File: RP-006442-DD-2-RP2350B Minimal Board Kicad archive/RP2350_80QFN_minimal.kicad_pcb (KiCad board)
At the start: 2 copper layers, 99.4 x 99.4 mm, 164 parts, among them J1 USB_C_Receptacle_USB2.0_16P, J2 Conn_02x14_Odd_Even, J3 Conn_02x09_Odd_Even, J4 Conn_01x03, J5 USB_C_Receptacle_USB2.0_16P, J6 Conn_01x05, SW1 SW_Push, SW10 SW_DIP_x08, SW2 SW_Push, SW3 SW_Push, SW4 SW_Push, SW5 SW_Push, SW6 SW_Push, SW7 SW_Push, SW8 SW_Push, SW9 SW_SPDT, U1 RP2350_80QFN, U10 74HC595, U11 74HC595, U12 LIS2DW12TR, U13 74HC595, U2 NCP1117-3.3_SOT223, U3 W25Q128JVS, U4 DNF, U5 W25Q128JVS, U6 NCP1117-3.3_SOT223, U7 RP2350_60QFN, U8 HT16K33A-24SSOP, U9 CC56-12EWA, Y1 ABM8-272-T3, Y2 ABM8-272-T3

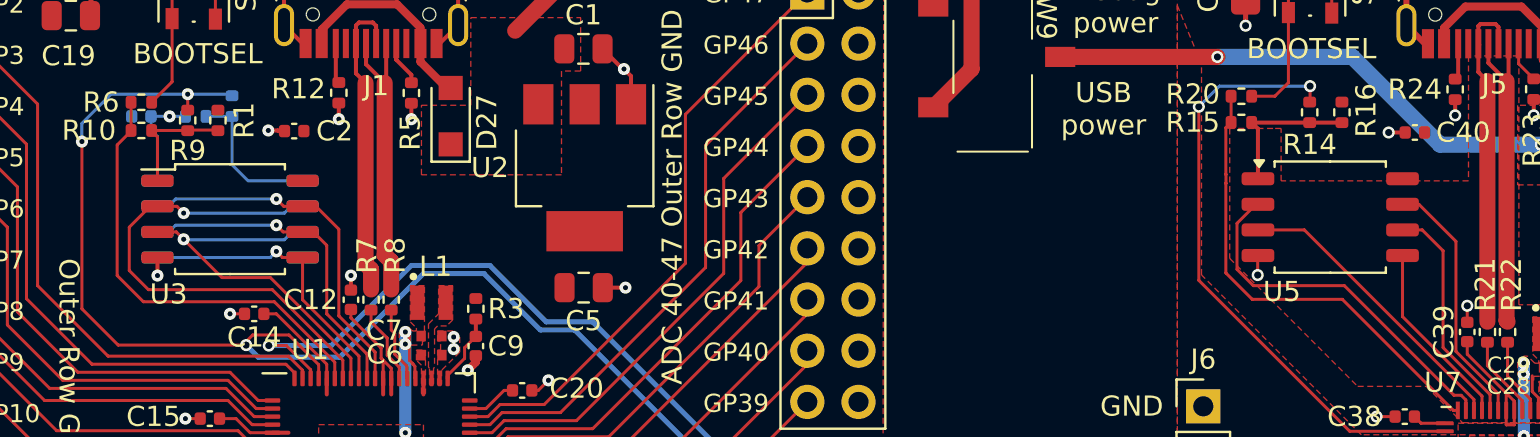
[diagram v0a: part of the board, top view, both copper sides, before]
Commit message: New Flash memory footprint
footprint from snapmagic
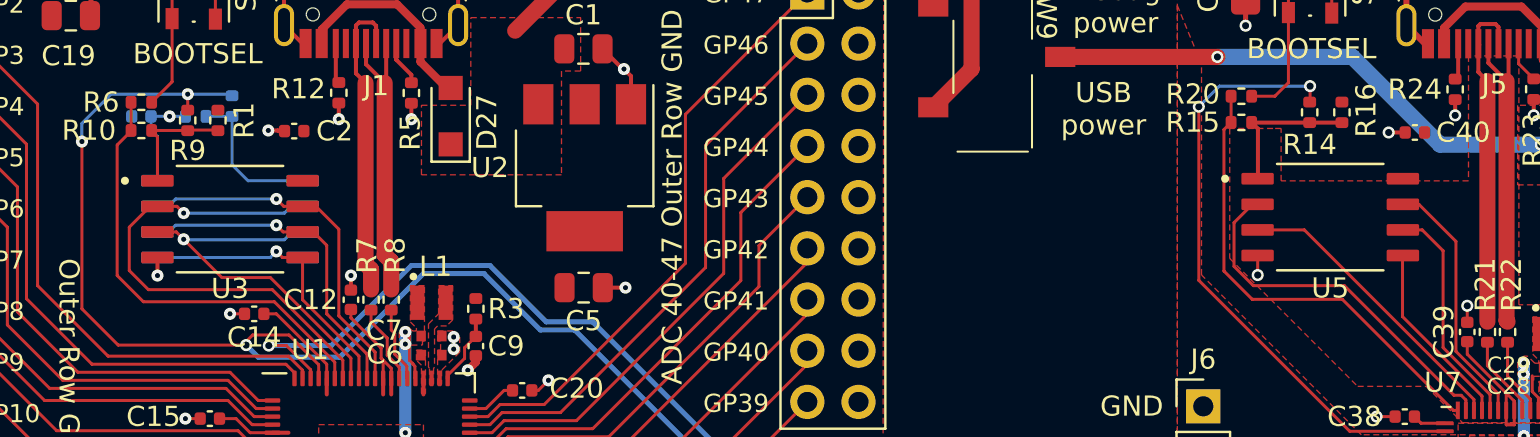
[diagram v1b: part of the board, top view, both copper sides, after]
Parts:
- U3, U4: footprint Package_SO:SOIC-8_5.23x5.23mm_P1.27mm -> W25Q128JVSIQ:SOIC127P790X216-8N
- U5: footprint Package_SO:SOIC-8_5.3x5.3mm_P1.27mm -> W25Q128JVSIQ:SOIC127P790X216-8N

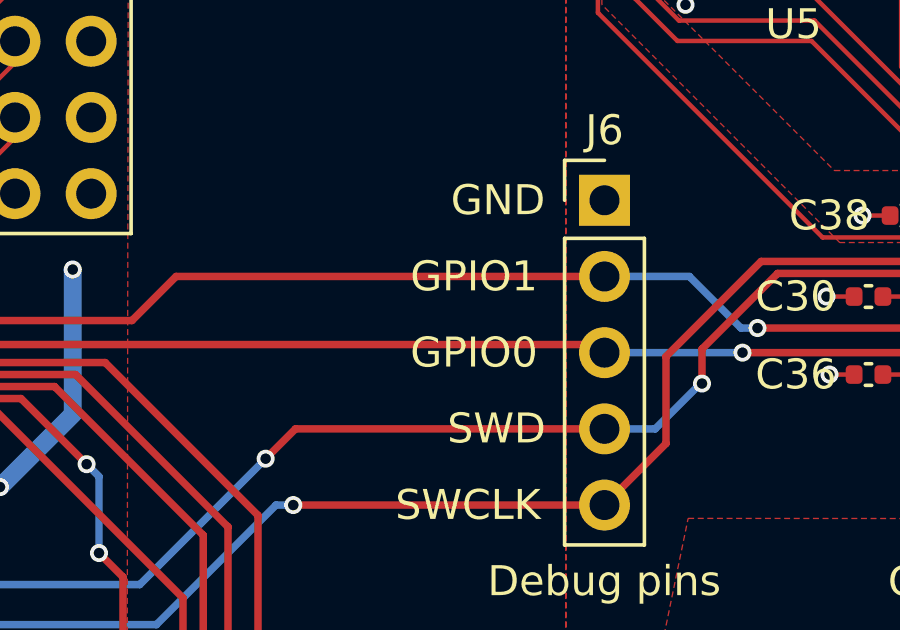
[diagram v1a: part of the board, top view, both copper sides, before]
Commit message: Added MMA8451QR1 symbol and footprint
MMA8451QR1 Accelerometer
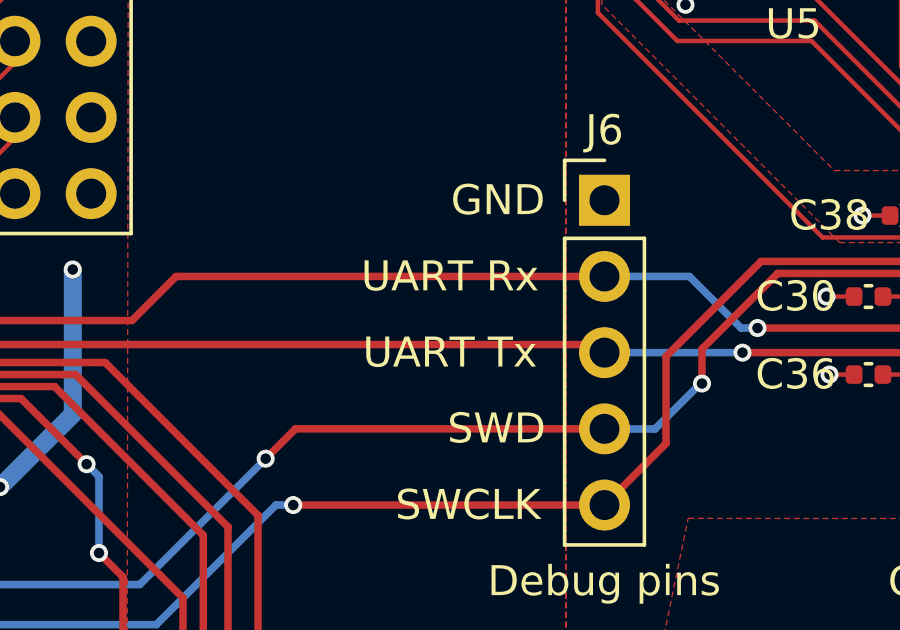
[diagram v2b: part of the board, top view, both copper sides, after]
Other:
- board text added: "UART Rx"
- board text added: "UART Tx"
- board text removed: "GPIO0"
- board text removed: "GPIO1"
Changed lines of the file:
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@@
 		)
 	)
-	(gr_text "GPIO1"
-		(at 124.8 74.08 0)
+	(gr_text "UART Rx"
+		(at 124 74.08 0)
 		(layer "F.SilkS")
 		(effects
@@
 		)
 	)
-	(gr_text "GPIO0"
-		(at 124.8 76.62 0)
+	(gr_text "UART Tx"
+		(at 124 76.62 0)
 		(layer "F.SilkS")
 		(effects

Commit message: Update RP2350_80QFN_minimal.kicad_pcb
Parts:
- removed the C42 at (70.0, 95.7)
- removed the U12 at (75.2, 90.9)
- added U13: MMA8451QR1, MMA8451QR1:QFN50P300X300X100-16N, F.Cu at (72.5, 115.5)
- C45: value 100n -> 4.7u
- C47: value 10u -> 100n
- moved C45 25.9 mm to (75.5, 116.0)
- moved C42 24.5 mm to (74.5, 113.0), turned to 0 degrees
- moved C47 23.9 mm to (73.0, 112.5), turned to 90 degrees
- renumbered C46 to C42, U13 to U12
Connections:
- C42 pad 1: Net-(U12-VDD_IO) -> +3V3
- C45 pad 1: Net-(U12-VDD_IO) -> +3V3
- C47 pad 1: Net-(U12-VDD_IO) -> Net-(U13-BYP)
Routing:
- net /GPIO18: track 18.3 -> 55.2 mm, vias 2 -> 4
- net /GPIO19: track 17.0 -> 49.5 mm, vias 2 -> 4
- net /GPIO20: track 50.5 -> 57.8 mm, vias 2 -> 0
- net +3V3: track 175.4 -> 182.5 mm, vias 17 -> 15
- net /GPIO21: track 48.3 -> 55.3 mm, vias 2 -> 4
- net Net-(U12-VDD_IO): track 4.34 -> 0.00 mm
- net GND: track 175.5 -> 179.2 mm, vias 104 -> 106
- net Net-(U13-BYP): track 0.00 -> 1.25 mm

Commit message: Update pcb
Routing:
- net +3V3: track 182.5 -> 185.0 mm, vias 15 -> 17
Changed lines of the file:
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@@
 			(psa4output no)
 			(plot_black_and_white yes)
+			(plotinvisibletext no)
 			(sketchpadsonfab no)
 			(plotpadnumbers no)
@@
 			(keep_text_aligned yes)
 		)
-		(gr_text "12,7000 mm"
+		(gr_text "12.7000 mm"
 			(at 92.35 148.2725 0)
 			(layer "Cmts.User")
@@
 			(keep_text_aligned yes)
 		)
-		(gr_text "2,0000 mm"
+		(gr_text "2.0000 mm"
 			(at 63.95 117.8 90)
 			(layer "Cmts.User")
@@
 			(keep_text_aligned yes)
 		)
-		(gr_text "17,7700 mm"
+		(gr_text "17.7700 mm"
 			(at 87.185 101.3 0)
 			(layer "Cmts.User")
@@
 			(keep_text_aligned yes)
 		)
-		(gr_text "10,4000 mm"
+		(gr_text "10.4000 mm"
 			(at 104.31 102.45 90)
 			(layer "Cmts.User")
@@
 			(keep_text_aligned yes)
 		)
-		(gr_text "50,3000 mm"
+		(gr_text "50.3000 mm"
 			(at 92.35 144.32 0)
 			(layer "Cmts.User")
@@
 			(keep_text_aligned yes)
 		)
-		(gr_text "19,0000 mm"
+		(gr_text "19.0000 mm"
 			(at 69.84 130.38 90)
 			(layer "Cmts.User")
@@
 			(keep_text_aligned yes)
 		)
-		(gr_text "2,5400 mm"
+		(gr_text "2.5400 mm"
 			(at 79.57 96.22 0)
 			(layer "Cmts.User")
@@
 			(keep_text_aligned yes)
 		)
-		(gr_text "7,4000 mm"
+		(gr_text "7.4000 mm"
 			(at 100.68 102.45 90)
 			(layer "Cmts.User")
@@
 			(keep_text_aligned yes)
 		)
-		(gr_text "15,2275 mm"
+		(gr_text "15.2275 mm"
 			(at 79.325 130.38625 90)
 			(layer "Cmts.User")
@@
 			(keep_text_aligned yes)
 		)
-		(gr_text "100,0000 mm"
+		(gr_text "100.0000 mm"
 			(at 180.55 95.05 90)
 			(layer "Cmts.User")
@@
 			(keep_text_aligned yes)
 		)
-		(gr_text "99,4000 mm"
+		(gr_text "99.4000 mm"
 			(at 111.85 36.55 0)
 			(layer "Cmts.User")
@@
 			(keep_text_aligned yes)
 		)
-		(gr_text "5,0000 mm"
+		(gr_text "5.0000 mm"
 			(at 74.1 142.5 90)
 			(layer "Cmts.User")
@@
 	)
 	(segment
-		(start 70.53 95.7)
-		(end 70.53 96.92)
-		(width 0.25)
-		(layer "F.Cu")
-		(net 5)
-	)
-	(segment
 		(start 85.25 79.9465)
 		(end 85.25 79.15)
@@
 	)
 	(segment
+		(start 70.53 95.5)
+		(end 69.58 94.55)
+		(width 0.25)
+		(layer "F.Cu")
+		(net 5)
+	)
+	(segment
 		(start 75.663806 115.414)
 		(end 76.286 115.414)
@@
 	)
 	(segment
-		(start 70.53 95.5)
-		(end 69.58 94.55)
-		(width 0.25)
-		(layer "F.Cu")
-		(net 5)
-	)
-	(segment
 		(start 112.95 116.97)
 		(end 122.75 126.77)
@@
 	)
 	(segment
-		(start 70.53 95.7)
-		(end 70.53 95.5)
-		(width 0.15)
-		(layer "F.Cu")
-		(net 5)
-	)
-	(segment
 		(start 84.5 57.9)
 		(end 84.52 57.88)
@@
 	)
 	(segment
+		(start 70.53 96.92)
+		(end 70.53 95.5)
+		(width 0.25)
+		(layer "F.Cu")
+		(net 5)
+	)
+	(segment
 		(start 144.58223 72.46)
 		(end 144.58223 71.7415)
@@
 	)
 	(segment
-		(start 70.53 96.92)
-		(end 70.35 97.1)
-		(width 0.25)
-		(layer "F.Cu")
-		(net 5)
-	)
-	(segment
 		(start 144.18223 71.7415)
 		(end 144.18223 72.45223)
@@
 	)
 	(via
+		(at 76.55 110.55)
+		(size 0.6)
+		(drill 0.35)
+		(layers "F.Cu" "B.Cu")
+		(free yes)
+		(net 5)
+	)
+	(via
 		(at 107.25 80.25)
 		(size 0.6)
@@
 	)
 	(via
-		(at 77.45 91.6)
+		(at 107.625 97.825)
 		(size 0.6)
 		(drill 0.35)
@@
 	)
 	(via
-		(at 107.625 97.825)
+		(at 71.1 98.05)
 		(size 0.6)
 		(drill 0.35)
@@
 	)
 	(via
-		(at 77.45 85.65)
+		(at 76.55 106.975)
 		(size 0.6)
 		(drill 0.35)
 		(layers "F.Cu" "B.Cu")
+		(free yes)
 		(net 5)
 	)
@@
 	)
 	(via
+		(at 76.275 98.05)
+		(size 0.6)
+		(drill 0.35)
+		(layers "F.Cu" "B.Cu")
+		(free yes)
+		(net 5)
+	)
+	(via
 		(at 149.45 50.1)
 		(size 0.6)
@@
 	)
 	(segment
-		(start 77.45 91.6)
-		(end 77.45 85.65)
+		(start 76.55 110.55)
+		(end 76.55 106.975)
 		(width 0.6)
 		(layer "B.Cu")
@@
 	)
 	(segment
+		(start 71.1 98.05)
+		(end 76.275 98.05)
+		(width 0.6)
+		(layer "B.Cu")
+		(net 5)
+	)
+	(segment
 		(start 81.35 83.55)
 		(end 78.85 83.55)
@@
 	)
 	(segment
-		(start 111.3 109.55)
-		(end 112.35 109.55)
+		(start 77.575 101.75)
+		(end 99.15 101.75)
 		(width 0.25)
 		(layer "F.Cu")
@@
 	)
 	(segment
-		(start 66.525 86.925)
-		(end 66.525 94.75)
+		(start 111.3 109.55)
+		(end 112.35 109.55)
 		(width 0.25)
 		(layer "F.Cu")
@@
 	)
 	(segment
-		(start 99.15 101.75)
-		(end 76.2 101.75)
+		(start 66.525 86.925)
+		(end 66.525 94.75)
 		(width 0.25)
 		(layer "F.Cu")
@@
 	)
 	(via
-		(at 76.2 101.75)
+		(at 77.575 101.75)
 		(size 0.6)
 		(drill 0.35)
@@
 	)
 	(segment
-		(start 106.25 101.75)
-		(end 111.3 106.8)
+		(start 69.875 101.75)
+		(end 66.525 98.4)
 		(width 0.25)
 		(layer "B.Cu")
@@
 	)
 	(segment
-		(start 99.15 101.75)
-		(end 106.25 101.75)
+		(start 106.25 101.75)
+		(end 111.3 106.8)
 		(width 0.25)
 		(layer "B.Cu")
@@
 	)
 	(segment
-		(start 111.3 106.8)
-		(end 111.3 109.55)
+		(start 66.525 98.4)
+		(end 66.525 94.75)
 		(width 0.25)
 		(layer "B.Cu")
@@
 	)
 	(segment
-		(start 76.2 101.75)
-		(end 69.875 101.75)
+		(start 99.15 101.75)
+		(end 106.25 101.75)
 		(width 0.25)
 		(layer "B.Cu")
@@
 	)
 	(segment
-		(start 69.875 101.75)
-		(end 66.525 98.4)
+		(start 77.575 101.75)
+		(end 69.875 101.75)
 		(width 0.25)
 		(layer "B.Cu")
@@
 	)
 	(segment
-		(start 66.525 98.4)
-		(end 66.525 94.75)
+		(start 111.3 106.8)
+		(end 111.3 109.55)
 		(width 0.25)
 		(layer "B.Cu")
@@
 	)
 	(segment
+		(start 99.1 100.025)
+		(end 77.525 100.025)
+		(width 0.25)
+		(layer "F.Cu")
+		(net 32)
+	)
+	(segment
 		(start 111.325 100.025)
 		(end 112.375 100.025)
@@
 	)
 	(segment
-		(start 99.1 100.025)
-		(end 76.2 100.025)
-		(width 0.25)
-		(layer "F.Cu")
-		(net 32)
-	)
-	(segment
 		(start 67.8 96.05)
 		(end 67.8 88.25)
@@
 	)
 	(via
-		(at 76.2 100.025)
+		(at 77.525 100.025)
 		(size 0.6)
 		(drill 0.35)
@@
 	)
 	(segment
-		(start 67.8 97.125)
-		(end 67.8 96.05)
+		(start 70.7 100.025)
+		(end 67.8 97.125)
 		(width 0.25)
 		(layer "B.Cu")
@@
 	)
 	(segment
-		(start 70.7 100.025)
-		(end 67.8 97.125)
+		(start 77.525 100.025)
+		(end 70.7 100.025)
 		(width 0.25)
 		(layer "B.Cu")
@@
 	)
 	(segment
-		(start 76.2 100.025)
-		(end 70.7 100.025)
+		(start 67.8 97.125)
+		(end 67.8 96.05)
 		(width 0.25)
 		(layer "B.Cu")
@@
 	)
 	(segment
+		(start 77.475 100.825)
+		(end 99.1 100.825)
+		(width 0.25)
+		(layer "F.Cu")
+		(net 33)
+	)
+	(segment
 		(start 112.35 105)
 		(end 112.375 105.025)
@@
 	)
 	(segment
-		(start 67.15 95.5)
-		(end 67.15 87.6)
-		(width 0.25)
-		(layer "F.Cu")
-		(net 33)
-	)
-	(segment
 		(start 99.1 100.825)
 		(end 99.125 100.85)
@@
 	)
 	(segment
-		(start 76.2 100.825)
-		(end 99.1 100.825)
+		(start 67.15 95.5)
+		(end 67.15 87.6)
 		(width 0.25)
 		(layer "F.Cu")
@@
 	)
 	(via
-		(at 76.2 100.825)
+		(at 77.475 100.825)
 		(size 0.6)
 		(drill 0.35)
@@
 	)
 	(segment
-		(start 107.2 100.85)
-		(end 111.35 105)
+		(start 67.15 97.85)
+		(end 67.15 95.5)
 		(width 0.25)
 		(layer "B.Cu")
@@
 	)
 	(segment
-		(start 70.125 100.825)
-		(end 67.15 97.85)
+		(start 107.2 100.85)
+		(end 111.35 105)
 		(width 0.25)
 		(layer "B.Cu")
@@
 	)
 	(segment
-		(start 67.15 97.85)
-		(end 67.15 95.5)
+		(start 70.125 100.825)
+		(end 67.15 97.85)
 		(width 0.25)
 		(layer "B.Cu")
@@
 	)
 	(segment
-		(start 76.2 100.825)
-		(end 70.125 100.825)
+		(start 99.125 100.85)
+		(end 107.2 100.85)
 		(width 0.25)
 		(layer "B.Cu")
@@
 	)
 	(segment
-		(start 99.125 100.85)
-		(end 107.2 100.85)
+		(start 77.475 100.825)
+		(end 70.125 100.825)
 		(width 0.25)
 		(layer "B.Cu")

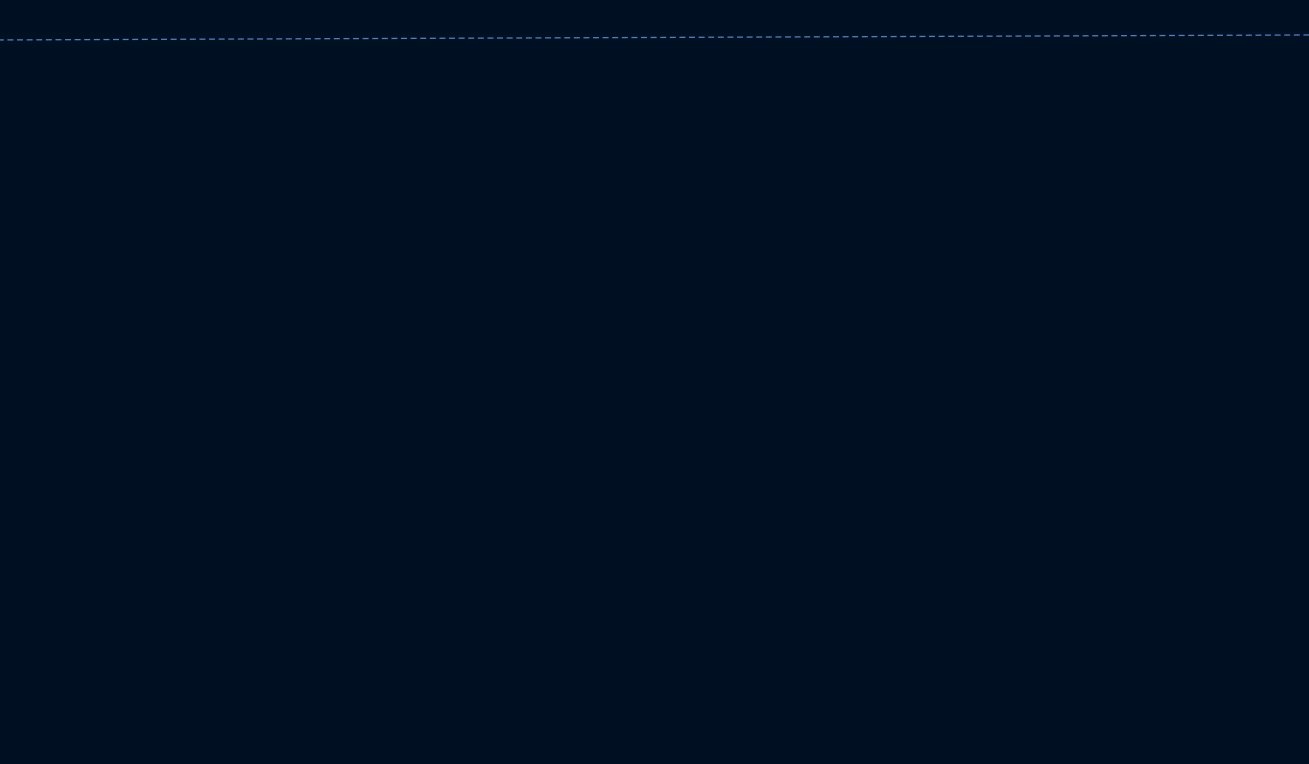
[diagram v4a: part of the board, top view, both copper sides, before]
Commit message: Update GS3011CR-G footprint
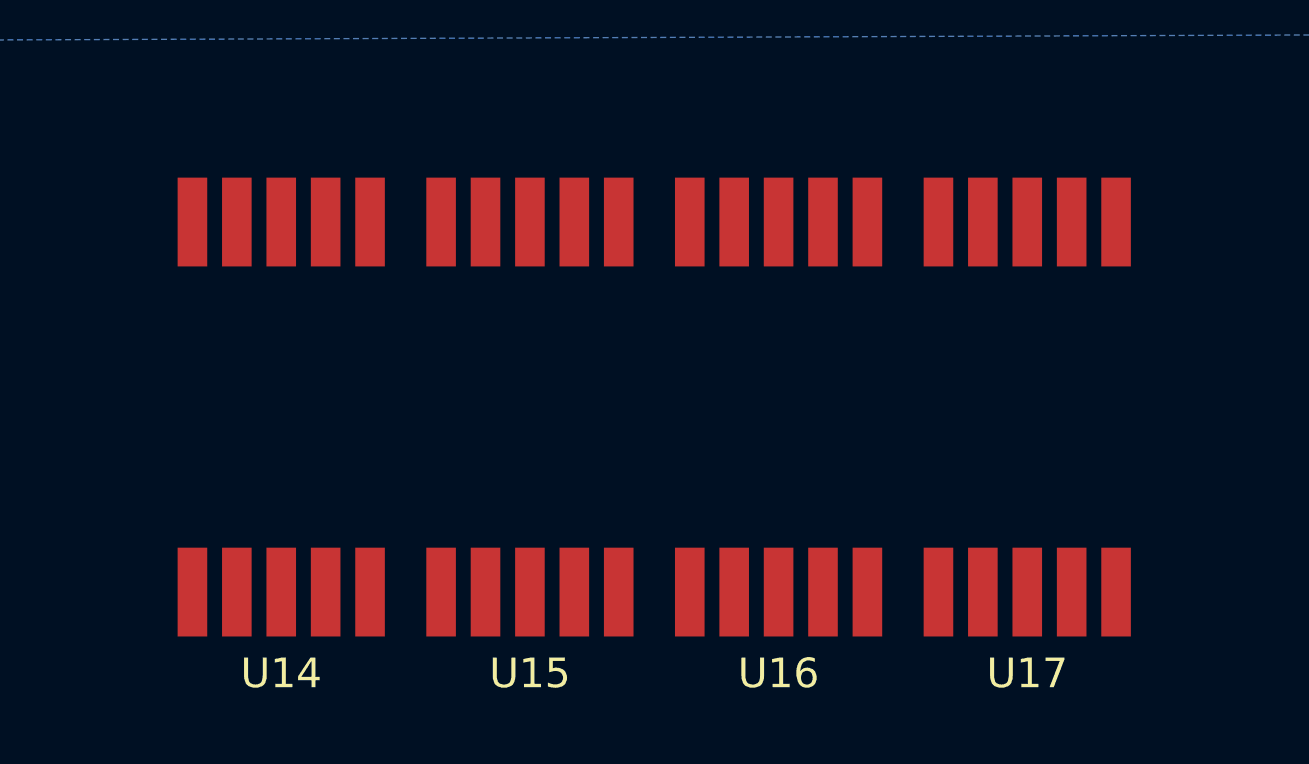
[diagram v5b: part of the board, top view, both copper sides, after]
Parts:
- added U14: GS3011CR-G, GS3011CR-G:GS3011CR-G, F.Cu at (83.6, 159.1)
- added U15: GS3011CR-G, GS3011CR-G:GS3011CR-G, F.Cu at (92.0, 159.1)
- added U16: GS3011CR-G, GS3011CR-G:GS3011CR-G, F.Cu at (100.4, 159.1)
- added U17: GS3011CR-G, GS3011CR-G:GS3011CR-G, F.Cu at (108.8, 159.1)
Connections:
- net /a' renamed /Accelerometer/SA0
- C10 pad 1: +1V1 -> +1V1_A
- C11 pad 1: +1V1 -> +1V1_A
- C12 pad 1: +3V3 -> +3V3_A
- C13 pad 1: +3V3 -> +3V3_A
- C14 pad 1: +3V3 -> +3V3_A
- C15 pad 1: +3V3 -> +3V3_A
- C16 pad 1: +3V3 -> +3V3_A
- C17 pad 1: +3V3 -> +3V3_A
- C18 pad 1: +3V3 -> +3V3_A
- C19 pad 1: +3V3 -> +3V3_A
- C2 pad 1: +3V3 -> +3V3_A
- C20 pad 1: +3V3 -> +3V3_A
- C21 pad 1: +3V3 -> +3V3_A
- C22 pad 1: +3V3 -> +3V3_A
- C23 pad 1: VDC -> /VSYS
- C42 pad 1: +3V3 -> +3V3_A
- C43 pad 1: +3V3 -> +3V3_A
- C44 pad 1: +3V3 -> +3V3_A
- C45 pad 1: +3V3 -> +3V3_A
- C48 pad 1: +3V3 -> +3V3_A
- C49 pad 1: +3V3 -> +3V3_A
- C5 pad 1: +3V3 -> +3V3_A
- C6 pad 1: +3V3 -> +3V3_A
- C7 pad 1: +1V1 -> +1V1_A
- C8 pad 1: +1V1 -> +1V1_A
- D27 pad 2: VBUS -> VBUS_A
- D28 pad 1: VDC -> /VSYS
- J1 pad A4: VBUS -> VBUS_A
- J1 pad A9: VBUS -> VBUS_A
- J1 pad B4: VBUS -> VBUS_A
- J1 pad B9: VBUS -> VBUS_A
- J2 pad 2: +3V3 -> +3V3_A
- L1 pad 1: +1V1 -> +1V1_A
- R1 pad 1: +3V3 -> +3V3_A
- R13 pad 1: +3V3 -> +3V3_A
- R26 pad 1: +3V3 -> +3V3_A
- R3 pad 1: +3V3 -> +3V3_A
- R43 pad 1: +3V3 -> +3V3_A
- SW9 pad 2: VDC -> /VSYS
- U1 pad 10: +1V1 -> +1V1_A
- U1 pad 15: +3V3 -> +3V3_A
- U1 pad 24: +3V3 -> +3V3_A
- U1 pad 29: +3V3 -> +3V3_A
- U1 pad 32: +1V1 -> +1V1_A
- U1 pad 41: +3V3 -> +3V3_A
- U1 pad 5: +3V3 -> +3V3_A
- U1 pad 50: +3V3 -> +3V3_A
- U1 pad 51: +1V1 -> +1V1_A
- U1 pad 59: +3V3 -> +3V3_A
- U1 pad 60: +3V3 -> +3V3_A
- U1 pad 64: +3V3 -> +3V3_A
- U1 pad 65: +1V1 -> +1V1_A
- U1 pad 68: +3V3 -> +3V3_A
- U1 pad 69: +3V3 -> +3V3_A
- U1 pad 76: +3V3 -> +3V3_A
- U10 pad 16: +3V3 -> +3V3_A
- U11 pad 16: +3V3 -> +3V3_A
- U12 pad 16: +3V3 -> +3V3_A
- U13 pad 1: +3V3 -> +3V3_A
- U13 pad 14: +3V3 -> +3V3_A
- U2 pad 2: +3V3 -> +3V3_A
- U3 pad 8: +3V3 -> +3V3_A
- U4 pad 8: +3V3 -> +3V3_A
- U6 pad 3: VDC -> /VSYS
- U8 pad 24: +3V3 -> +3V3_A
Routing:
- net +3V3_A: track 0.00 -> 146.3 mm, vias 0 -> 1
- net +3V3: track 185.0 -> 38.7 mm, vias 17 -> 16
- net +1V1_A: track 0.00 -> 30.2 mm, vias 0 -> 5
- net +1V1: track 55.7 -> 25.5 mm, vias 18 -> 13
- net VDC: track 25.7 -> 0.00 mm, vias 2 -> 0
- net /VSYS: track 33.4 -> 59.0 mm, vias 0 -> 2
- net VBUS_A: track 0.00 -> 10.3 mm
- net VBUS: track 20.6 -> 10.2 mm
- removed copper zone on F.Cu, net VDC
